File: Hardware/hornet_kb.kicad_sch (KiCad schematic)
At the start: 18 parts, among them J1 Conn_ST_STDC14, J10 USB_C_Receptacle_USB2.0, U1 nRF52840, Y1 32.768kHz, Y2 32MHz

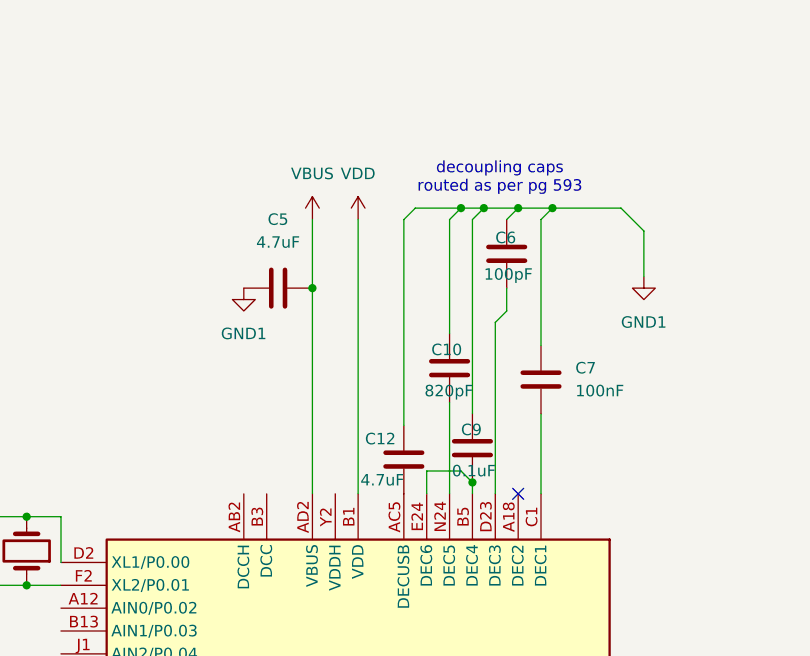
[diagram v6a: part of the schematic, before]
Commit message: Draft and spec out power components
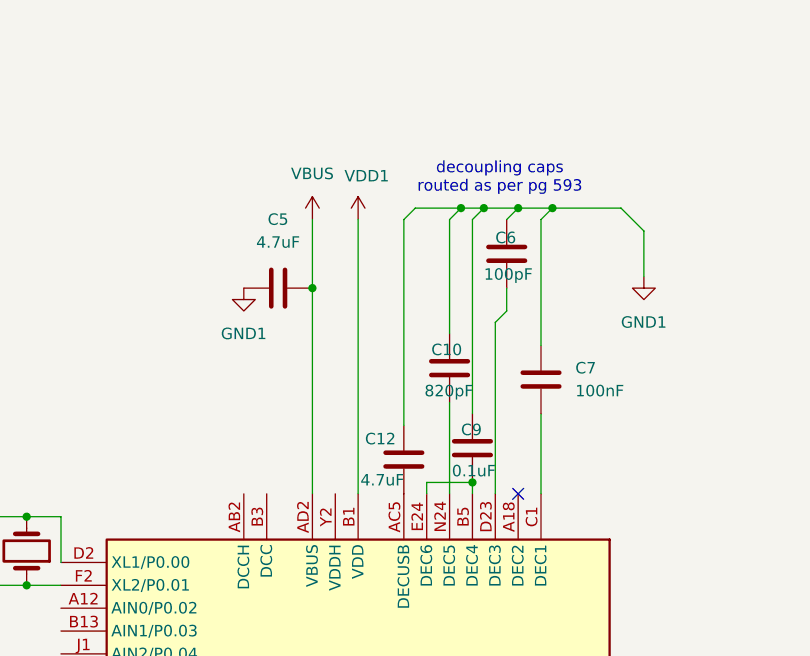
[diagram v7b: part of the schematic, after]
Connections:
- net VDD renamed VDD1
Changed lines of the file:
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@@
 	(wire
 		(pts
-			(xy 355.6 80.01) (xy 359.41 80.01)
+			(xy 355.6 81.28) (xy 360.68 81.28)
 		)
 		(stroke
@@
 	(wire
 		(pts
-			(xy 360.68 81.28) (xy 359.41 80.01)
-		)
-		(stroke
-			(width 0)
-			(type default)
-		)
-	)
-	(wire
-		(pts
 			(xy 358.14 52.07) (xy 359.41 50.8)
 		)
@@
 	(wire
 		(pts
-			(xy 355.6 80.01) (xy 355.6 82.55)
+			(xy 355.6 81.28) (xy 355.6 82.55)
 		)
 		(stroke
@@
 		(on_board yes)
 		(dnp no)
-		(fields_autoplaced yes)
 		(property "Reference" "#PWR08"
 			(at 347.98 55.88 0)
@@
 			)
 		)
-		(property "Value" "VDD"
-			(at 347.98 46.99 0)
+		(property "Value" "VDD1"
+			(at 346.456 47.244 0)
 			(effects
 				(font
 					(size 1.27 1.27)
 				)
+				(justify left)
 			)
 		)

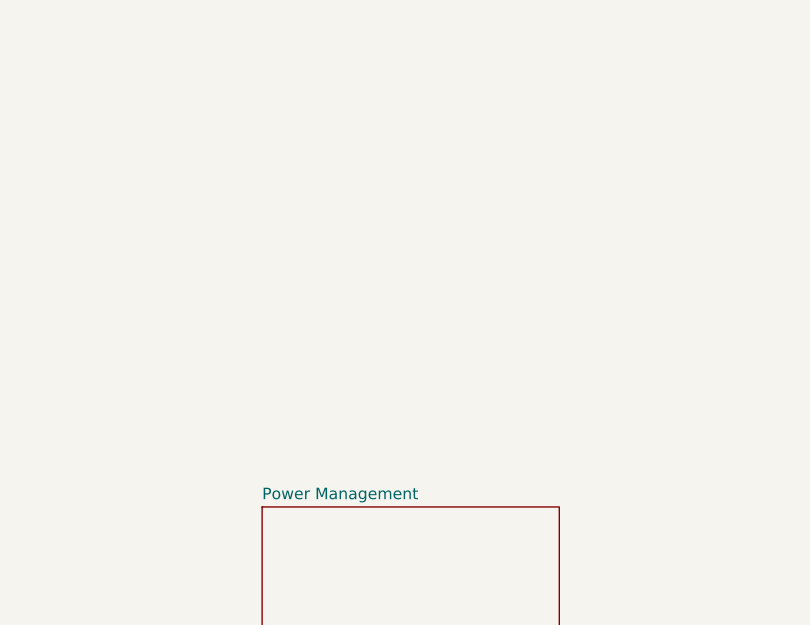
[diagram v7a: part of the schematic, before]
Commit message: Moved BLE implementation into higherarchical page
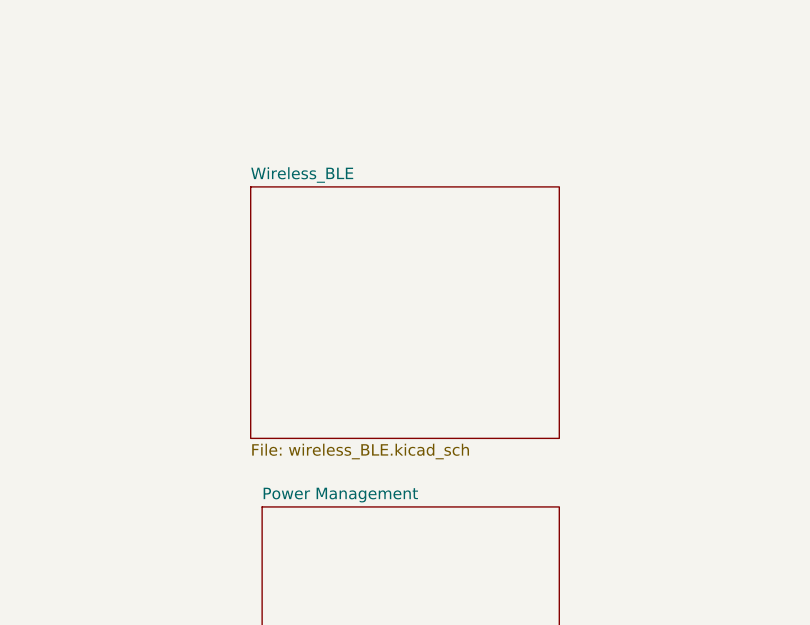
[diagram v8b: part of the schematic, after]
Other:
- added sheet Wireless_BLE (wireless_BLE.kicad_sch)
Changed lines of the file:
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@@
+	)
+	(sheet
+		(at 177.8 161.29)
+		(size 34.29 27.94)
+		(exclude_from_sim no)
+		(in_bom yes)
+		(on_board yes)
+		(dnp no)
+		(fields_autoplaced yes)
+		(stroke
+			(width 0.1524)
+			(type solid)
+		)
+		(fill
+			(color 0 0 0 0.0000)
+		)
+		(property "Sheetname" "Wireless_BLE"
+			(at 177.8 160.5784 0)
+			(effects
+				(font
+					(size 1.27 1.27)
+				)
+				(justify left bottom)
+			)
+		)
+		(property "Sheetfile" "wireless_BLE.kicad_sch"
+			(at 177.8 189.8146 0)
+			(effects
+				(font
+					(size 1.27 1.27)
+				)
+				(justify left top)
+			)
+		)
+		(instances
+			(project "hornet_kb"
+				(path "/c35084ab-104c-4a4c-9388-a839989b8e3d"
+					(page "4")
+				)
+			)
+		)
 	)
 	(sheet
